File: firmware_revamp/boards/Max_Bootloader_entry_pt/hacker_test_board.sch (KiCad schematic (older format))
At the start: 28 parts, among them J1 CONN_02X03, U1 MCP2561-E_SN, U2 ATMEGA16M1, Y1 Crystal_SMD

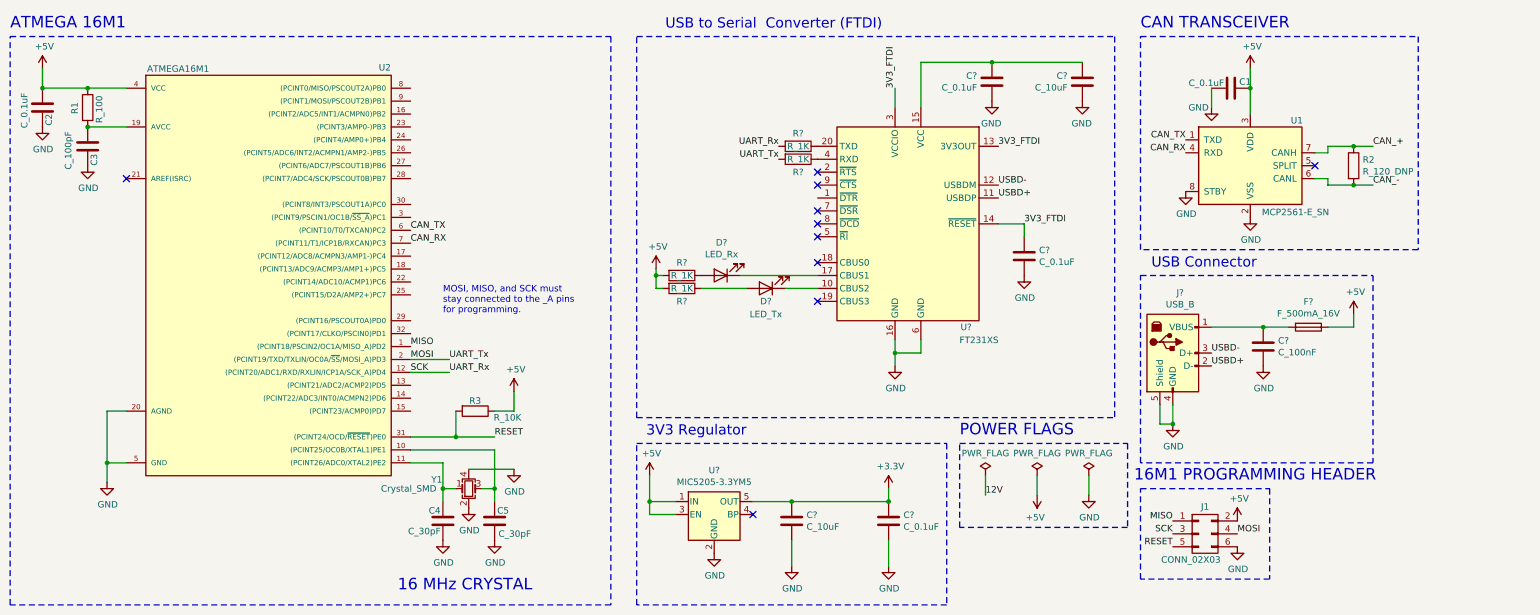
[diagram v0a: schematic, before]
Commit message: Completed first layout draft of Bootloader board
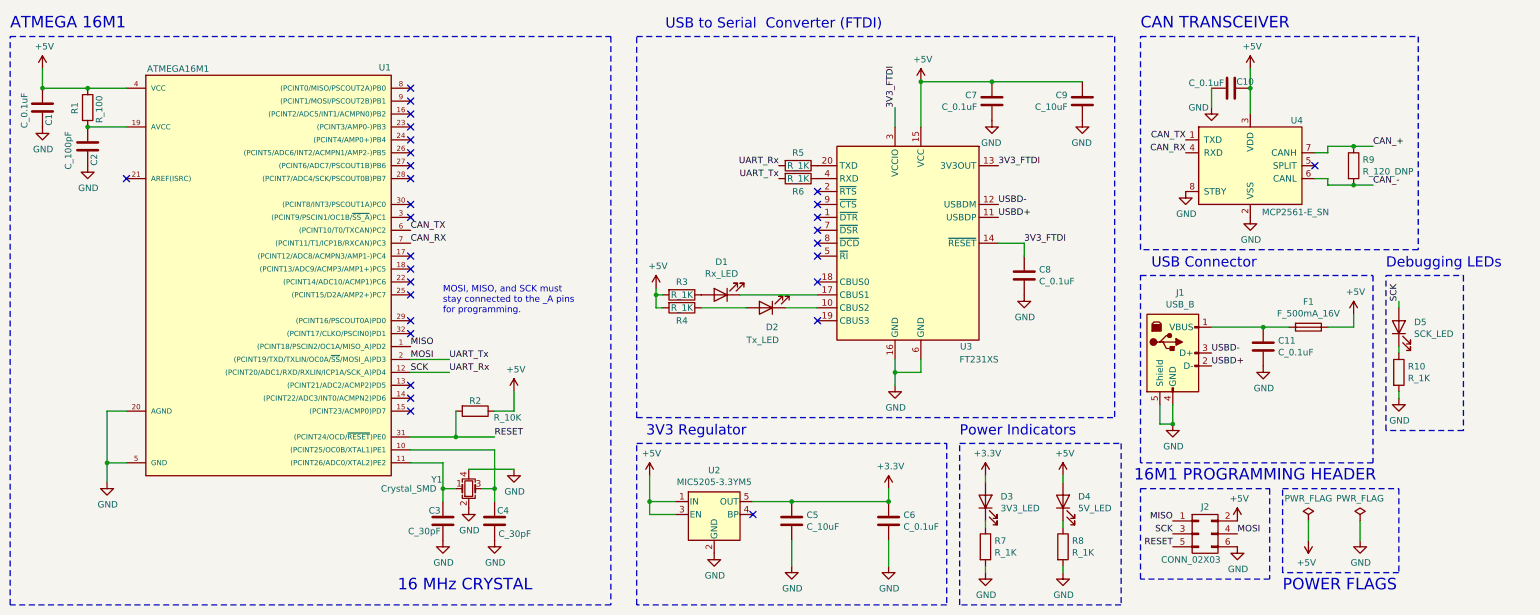
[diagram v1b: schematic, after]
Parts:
- removed C?: C_100nF, footprints:C_0603_1608Metric, symbol formula:C_100nF
- removed D?: LED_Rx, symbol Device:LED
- removed D?: LED_Tx, symbol Device:LED
- removed J?: USB_B, symbol Connector:USB_B
- added C11: C_0.1uF, footprints:C_0805_OEM, symbol formula:C_0.1uF
- added D1: Rx_LED, footprints:LED_0805_OEM, symbol formula:LED_0805
- added D2: Tx_LED, footprints:LED_0805_OEM, symbol formula:LED_0805
- added D3: 3V3_LED, footprints:LED_0805_OEM, symbol formula:LED_0805
- added D4: 5V_LED, footprints:LED_0805_OEM, symbol formula:LED_0805
- added D5: SCK_LED, footprints:LED_0805_OEM, symbol formula:LED_0805
- added J1: USB_B, Connector_USB:USB_B_Lumberg_2411_02_Horizontal, symbol Connector:USB_B
- added R10, R7, R8: R_1K, footprints:R_0805_OEM, symbol formula:R_1K
- gave numbers to parts that had none: 12
- renumbered C2 to C1, C1 to C10, C3 to C2, C4 to C3, C5 to C4, J1 to J2, R3 to R2, R2 to R9, U2 to U1, U1 to U4
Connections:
- net +3V3: now also D3.2 (A)
- net +5V: now also C7.1, C9.1, U3.15 (VCC), D4.2 (A)
- net GND: now also C11.2, J1.4 (GND), J1.5 (Shield), R10.2, R7.2, R8.2
- net SCK: now also D5.2 (A)
- net USBD+: now also J1.2 (D-)
- net USBD-: now also J1.3 (D+)
- net at F1.2: now also C11.1, J1.1 (VBUS)
- net at U3.10 (CBUS2): now also D2.1 (K)
- net at U3.17 (CBUS1): now also D1.1 (K)
- net at R3.1: now also D1.2 (A)
- net at R4.1: now also D2.2 (A)
- new net: D3.1 (K), R7.1
- new net: D4.1 (K), R8.1
- new net: D5.1 (K), R10.1
- no-connect marks 10 -> 30
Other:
- note added: "Debugging LEDs"
- note added: "Power Indicators"
- moved on the sheet: C7, C8, C9, R3, R4, R5, R6, U3
